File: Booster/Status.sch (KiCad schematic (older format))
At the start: 35 parts

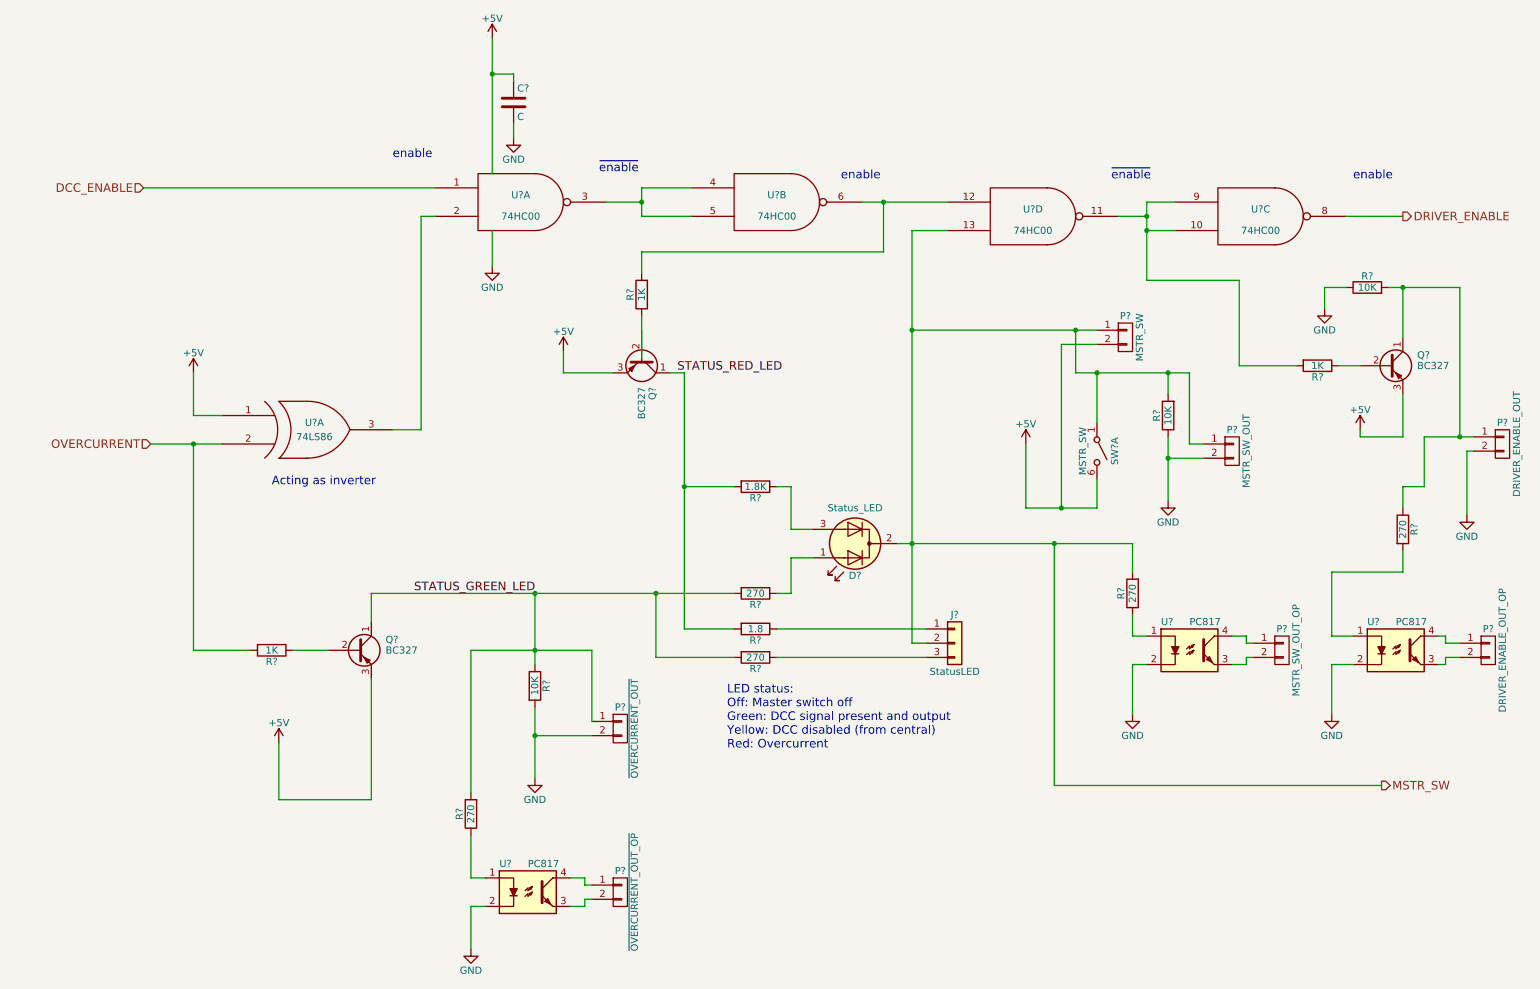
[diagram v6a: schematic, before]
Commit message: Using spare xor gate to make all transistors PNP types.
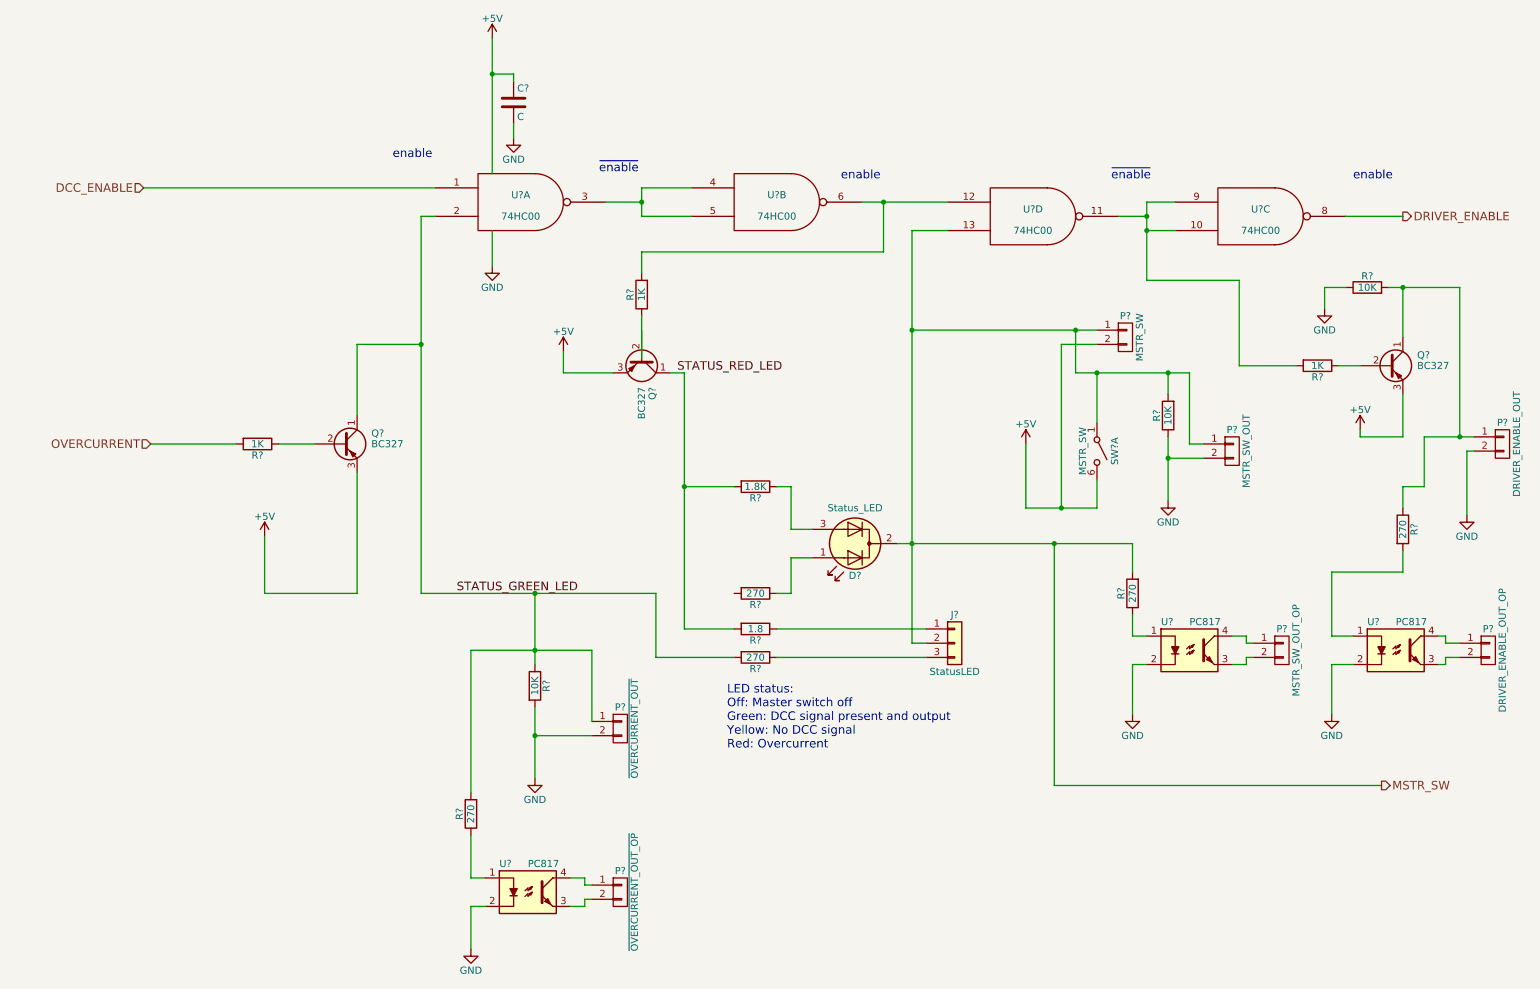
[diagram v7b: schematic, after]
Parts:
- removed U?: 74LS86, symbol 74LS86
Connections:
- net STATUS_GREEN_LED: now also U?.2; no longer R?.2
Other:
- note added: "LED status:\nOff: Master switch off\nGreen: DCC signal present and output\nYellow: No DCC signal\nRed: Overcurrent"
- note removed: "Acting as inverter"
- note removed: "LED status:\nOff: Master switch off\nGreen: DCC signal present and output\nYellow: DCC disabled (from central)\nRed: Overcurrent"
- moved on the sheet: Q?, R?
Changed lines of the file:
@@
 DRIVER_ENABLE
 Text Notes 5500 5800 0    60   ~ 0
-LED status:\nOff: Master switch off\nGreen: DCC signal present and output\nYellow: DCC disabled (from central)\nRed: Overcurrent
+LED status:\nOff: Master switch off\nGreen: DCC signal present and output\nYellow: No DCC signal\nRed: Overcurrent
 $Comp
 L LED_Dual_ACA D?
@@
 L BC327 Q?
 U 1 1 5A0BE3D7
-P 2900 5100
-F 0 "Q?" H 3100 5175 50  0000 L CNN
-F 1 "BC327" H 3100 5100 50  0000 L CNN
-F 2 "TO_SOT_Packages_THT:TO-92_Molded_Narrow" H 3100 5025 50  0001 L CIN
-F 3 "" H 2900 5100 50  0001 L CNN
-	1    2900 5100
+P 2800 3650
+F 0 "Q?" H 3000 3725 50  0000 L CNN
+F 1 "BC327" H 3000 3650 50  0000 L CNN
+F 2 "TO_SOT_Packages_THT:TO-92_Molded_Narrow" H 3000 3575 50  0001 L CIN
+F 3 "" H 2800 3650 50  0001 L CNN
+	1    2800 3650
 	1    0    0    -1
 $EndComp
@@
 L R R?
 U 1 1 5A0BE434
-P 2300 5100
-F 0 "R?" V 2380 5100 50  0000 C CNN
-F 1 "1K" V 2300 5100 50  0000 C CNN
-F 2 "" V 2230 5100 50  0001 C CNN
-F 3 "" H 2300 5100 50  0001 C CNN
-	1    2300 5100
+P 2200 3650
+F 0 "R?" V 2280 3650 50  0000 C CNN
+F 1 "1K" V 2200 3650 50  0000 C CNN
+F 2 "" V 2130 3650 50  0001 C CNN
+F 3 "" H 2200 3650 50  0001 C CNN
+	1    2200 3650
 	0    1    1    0
 $EndComp
@@
 L +5V #PWR?
 U 1 1 5A0BE54E
-P 2350 5750
-F 0 "#PWR?" H 2350 5600 50  0001 C CNN
-F 1 "+5V" H 2350 5890 50  0000 C CNN
-F 2 "" H 2350 5750 50  0001 C CNN
-F 3 "" H 2350 5750 50  0001 C CNN
-	1    2350 5750
+P 2250 4300
+F 0 "#PWR?" H 2250 4150 50  0001 C CNN
+F 1 "+5V" H 2250 4440 50  0000 C CNN
+F 2 "" H 2250 4300 50  0001 C CNN
+F 3 "" H 2250 4300 50  0001 C CNN
+	1    2250 4300
 	1    0    0    -1
 $EndComp
@@
 	0    1    1    0
 $EndComp
-Text Label 3300 4700 0    60   ~ 0
+Text Label 3600 4700 0    60   ~ 0
 STATUS_GREEN_LED
 Text Label 5150 3150 0    60   ~ 0
@@
 F 3 "" H 3700 7200 50  0001 C CNN
 	1    3700 7200
-	1    0    0    -1
-$EndComp
-$Comp
-L 74LS86 U?
-U 1 1 5A0F5EBC
-P 2550 3550
-F 0 "U?" H 2600 3600 50  0000 C CNN
-F 1 "74LS86" H 2600 3500 50  0000 C CNN
-F 2 "" H 2550 3550 50  0001 C CNN
-F 3 "" H 2550 3550 50  0001 C CNN
-	1    2550 3550
 	1    0    0    -1
 $EndComp
@@
 $EndComp
 Wire Wire Line
-	1750 3650 1750 5100
-Wire Wire Line
 	6800 2150 7050 2150
 Wire Wire Line
@@
 Connection ~ 7950 2850
 Wire Wire Line
-	1750 5100 2150 5100
-Connection ~ 1750 3650
-Wire Wire Line
-	2450 5100 2700 5100
-Wire Wire Line
-	3000 5300 3000 6150
-Wire Wire Line
-	3000 6150 2350 6150
-Wire Wire Line
-	2350 6150 2350 5750
-Wire Wire Line
-	3000 4900 3000 4700
-Wire Wire Line
-	3000 4700 5550 4700
+	1450 3650 2050 3650
+Wire Wire Line
+	2350 3650 2600 3650
+Wire Wire Line
+	2900 3850 2900 4700
+Wire Wire Line
+	2900 4700 2250 4700
+Wire Wire Line
+	2250 4700 2250 4300
+Wire Wire Line
+	2900 2950 2900 3450
 Wire Wire Line
 	6100 4250 5950 4250
@@
 	5000 5150 5550 5150
 Wire Wire Line
-	5000 5150 5000 4700
-Connection ~ 5000 4700
+	5000 4700 5000 5150
 Wire Wire Line
 	6700 4350 8350 4350
@@
 	3700 6900 3700 7200
 Wire Wire Line
-	3350 2050 3350 3550
+	3350 2050 3350 4700
 Wire Wire Line
 	3350 2050 3450 2050
@@
 	6600 2300 6600 1950
 Connection ~ 6600 1950
-Wire Wire Line
-	1450 3650 1950 3650
-Wire Wire Line
-	3350 3550 3150 3550
-Text Notes 2300 3950 0    60   ~ 0
-Acting as inverter
 Wire Wire Line
 	7800 4350 7800 6050
@@
 Text HLabel 10100 6050 2    60   Output ~ 0
 MSTR_SW
-Wire Wire Line
-	1950 3450 1750 3450
-Wire Wire Line
-	1750 3450 1750 3150
-$Comp
-L +5V #PWR?
-U 1 1 5A390297
-P 1750 3150
-F 0 "#PWR?" H 1750 3000 50  0001 C CNN
-F 1 "+5V" H 1750 3290 50  0000 C CNN
-F 2 "" H 1750 3150 50  0000 C CNN
-F 3 "" H 1750 3150 50  0000 C CNN
-	1    1750 3150
-	1    0    0    -1
-$EndComp
 Wire Wire Line
 	1400 1850 3450 1850
@@
 Text Notes 9900 1800 0    60   ~ 0
 enable
+Wire Wire Line
+	3350 4700 5000 4700
+Wire Wire Line
+	2900 2950 3350 2950
+Connection ~ 3350 2950
 $EndSCHEMATC

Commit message: Fixed missing connections.
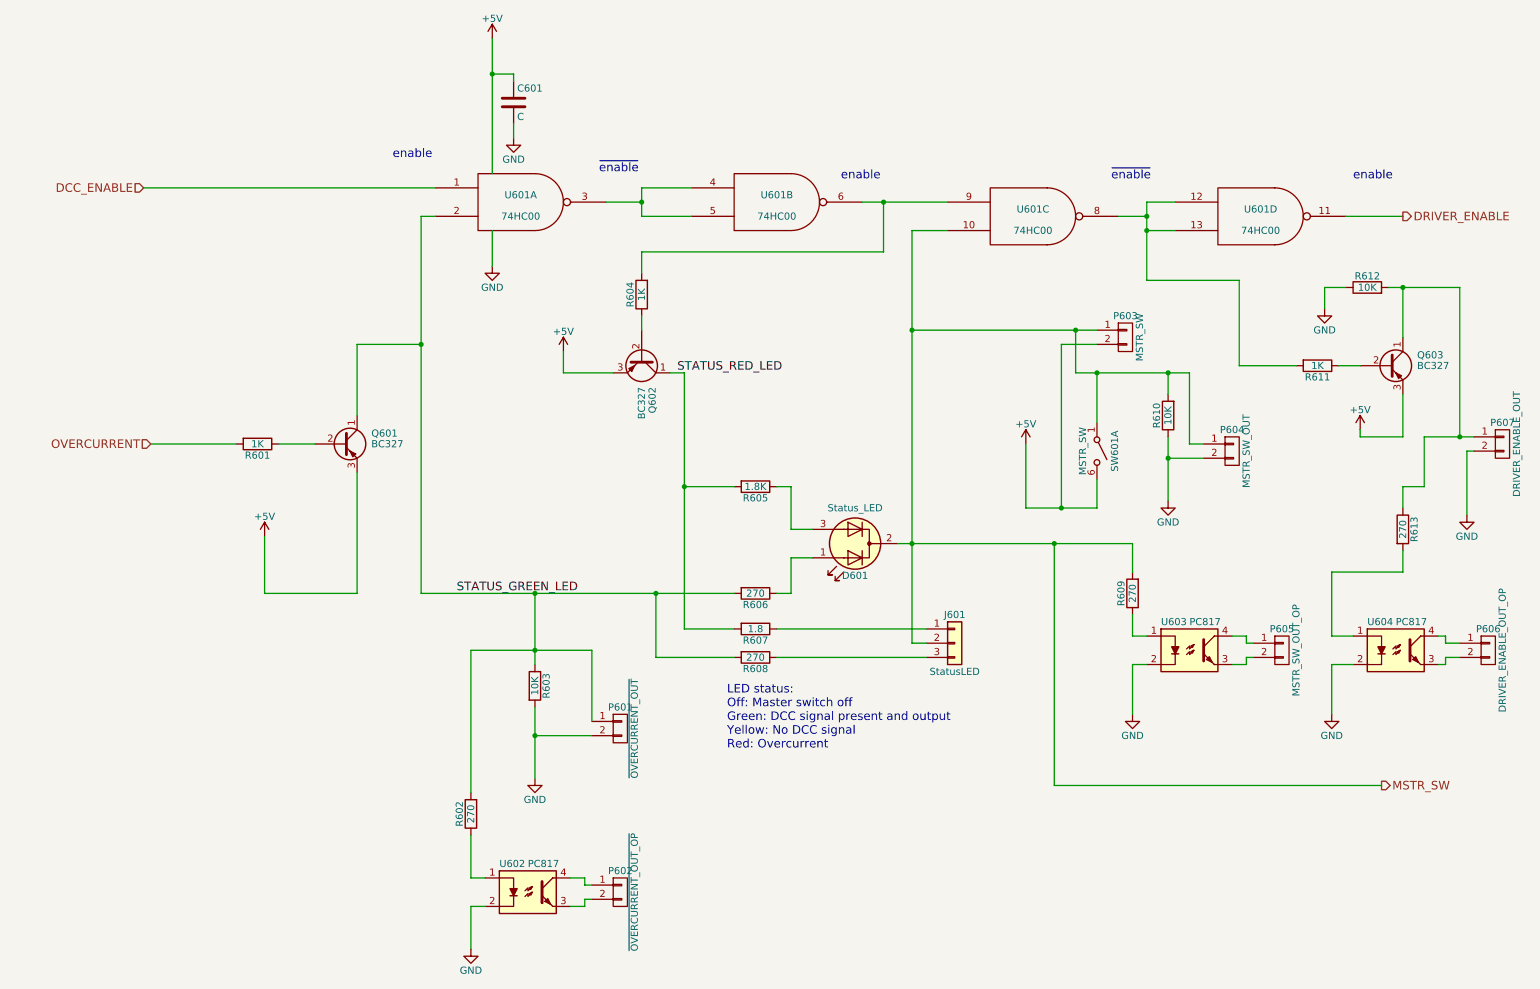
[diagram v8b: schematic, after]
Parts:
- gave numbers to parts that had none: 31
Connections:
- net DRIVER_ENABLE: now also U601.11; no longer U601.8
- net MSTR_SW: now also U601.10; no longer U601.13
- net STATUS_GREEN_LED: now also R606.2
- net at R604.1: now also Q602.2 (B)
- net at R604.2, U601.6: now also U601.9; no longer U601.12
- new net: R611.2, U601.12, U601.13, U601.8
